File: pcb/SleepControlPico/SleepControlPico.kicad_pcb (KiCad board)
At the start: 4 copper layers, 40 x 62 mm, 27 parts, among them J1 Display, J2 USB_C_Receptacle_USB2.0, J3 Conn_01x03, J4 Photodiode, SW1 RotaryEncoder_Switch, SW2 Boot, U1 AMS1117-33, U2 ESP32-S3-MINI-1-N8, U3 USBLC6-2SC6

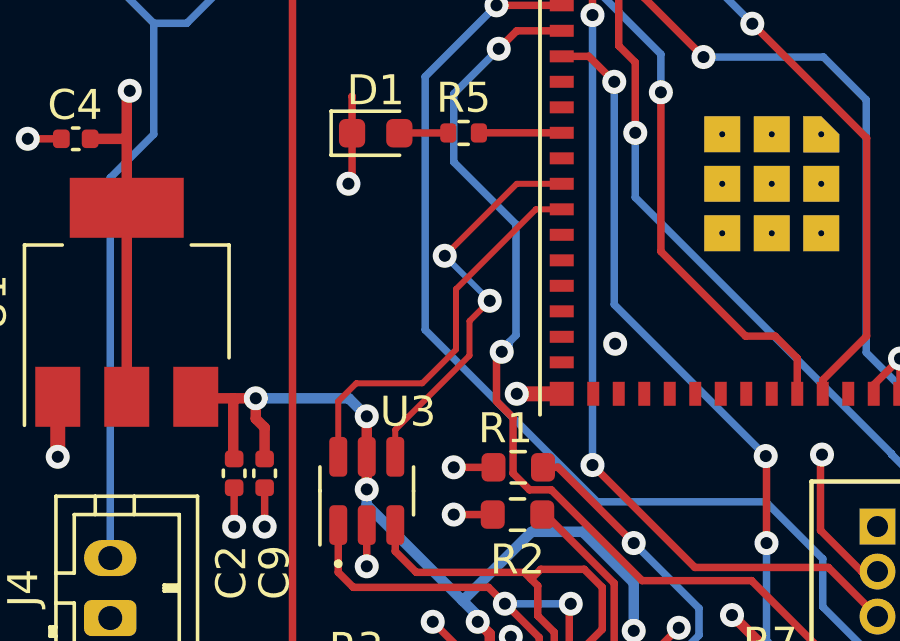
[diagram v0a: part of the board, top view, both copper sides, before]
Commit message: Fix USB D+ and D- lines being switched
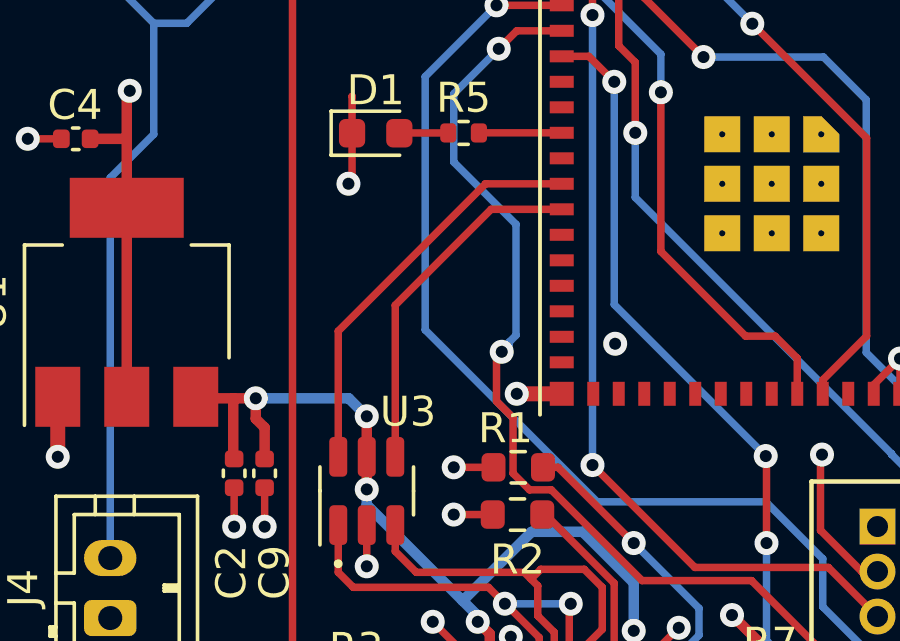
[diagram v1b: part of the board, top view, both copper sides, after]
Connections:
- J2 pad A6: /USB_D- -> /USB_D+
- J2 pad A7: /USB_D+ -> /USB_D-
- J2 pad B6: /USB_D- -> /USB_D+
- J2 pad B7: /USB_D+ -> /USB_D-
- U3 pad 1: /USB_D+ -> /USB_D-
- U3 pad 3: /USB_D- -> /USB_D+
- U3 pad 4: Net-(U2-IO19) -> Net-(U2-IO20)
- U3 pad 6: Net-(U2-IO20) -> Net-(U2-IO19)
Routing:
- net Net-(U2-IO20): track 13.1 -> 11.9 mm
- net /USB_D-: track 16.0 -> 15.8 mm, vias 0 -> 2
- net /USB_D+: track 15.8 -> 16.0 mm, vias 2 -> 0
- net Net-(U2-IO19): track 13.5 -> 13.7 mm, vias 2 -> 0
